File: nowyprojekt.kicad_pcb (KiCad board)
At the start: 4 copper layers, 75.6 x 70.8 mm, 46 parts, among them J1 Zasilanie, J2 01x03, J3 Conn_01x15_Pin, J4 Conn_01x15_Pin, Q1 BC856, Q2 BC856, Q3 BC856, Q4 BC856, U1 CA56-12SURKWA, U2 ATMEGA328P-AU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

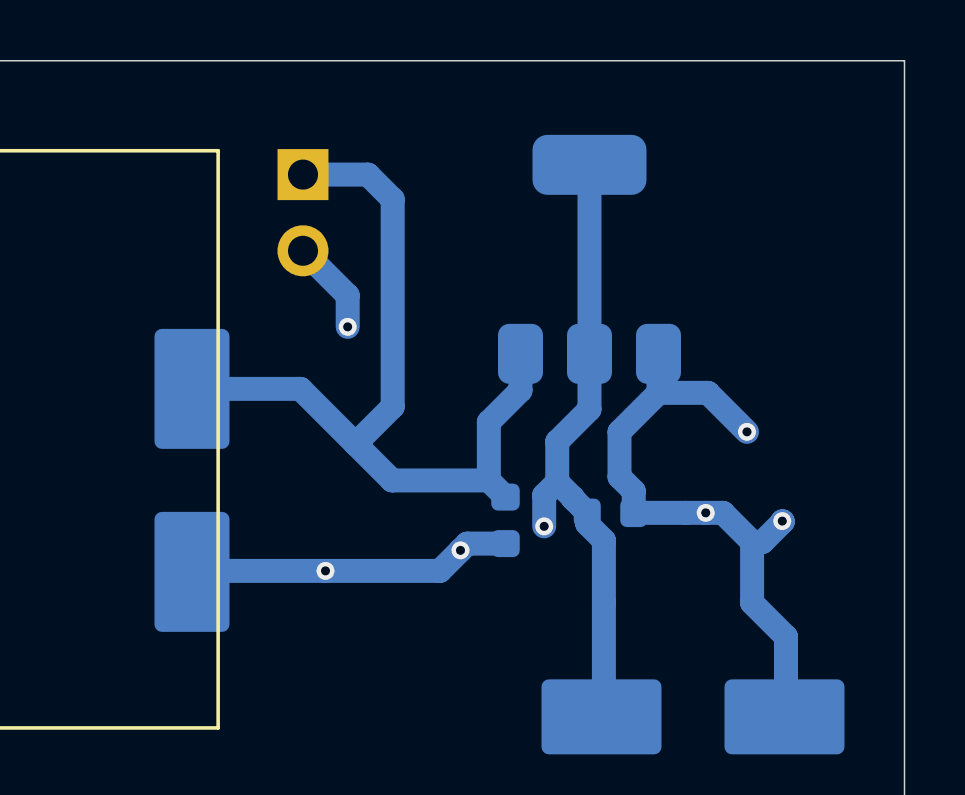
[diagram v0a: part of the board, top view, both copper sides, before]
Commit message: Inne rozwiazanie prowadzenia sciezek, z mysleniem zgodnym z 4 warstwami plytki... przelotki zasilania stabilizatora obok przelotek kondensatorow itd
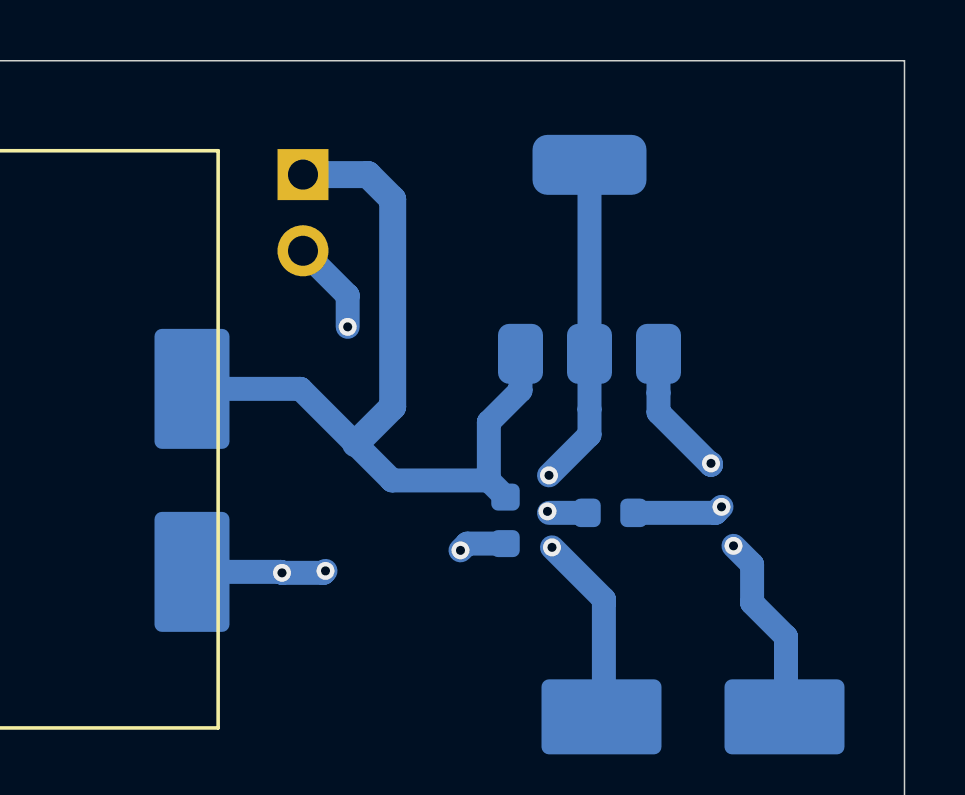
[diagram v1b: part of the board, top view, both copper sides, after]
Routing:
- net GND: track 82.9 -> 70.6 mm, vias 26 -> 27
- net +5V: track 66.7 -> 63.8 mm, vias 15 -> 17

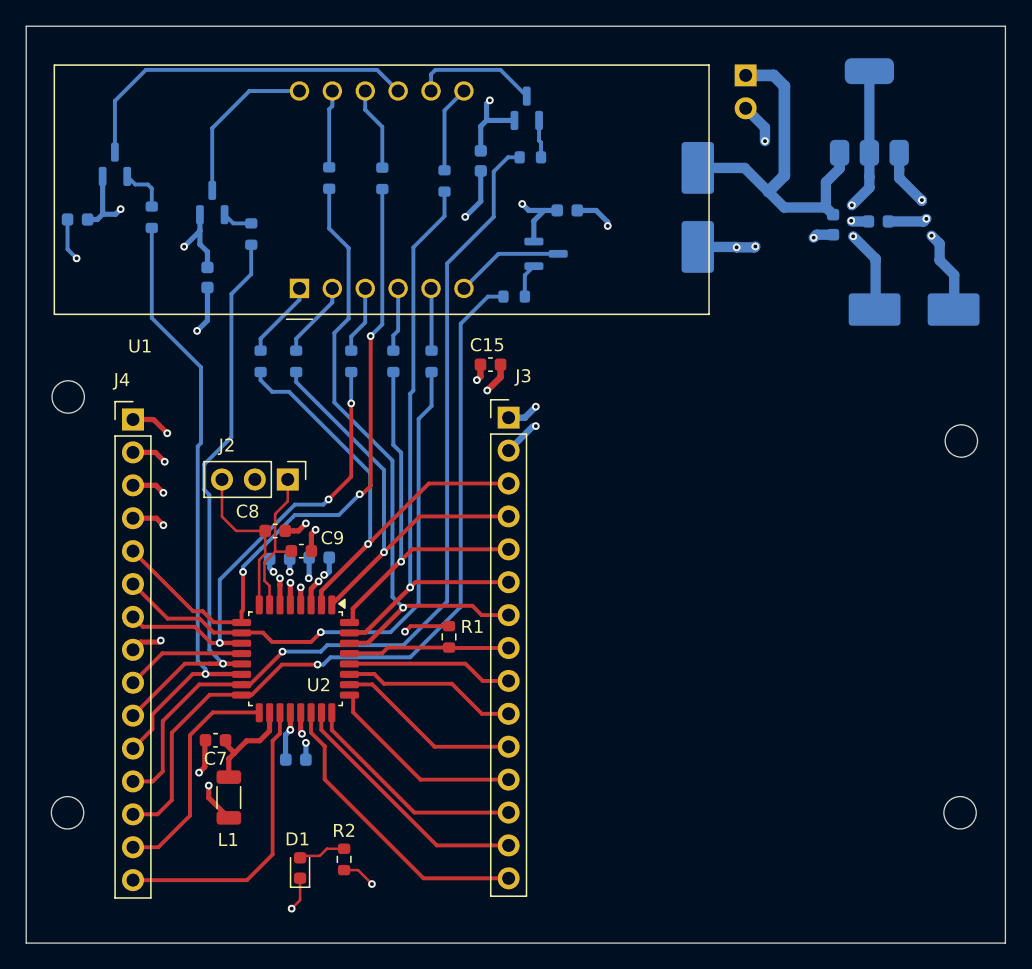
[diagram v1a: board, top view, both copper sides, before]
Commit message: 01.03.2026r zmiana prowadzenia sciezek - myslenie pod 4 warstwowe pcb
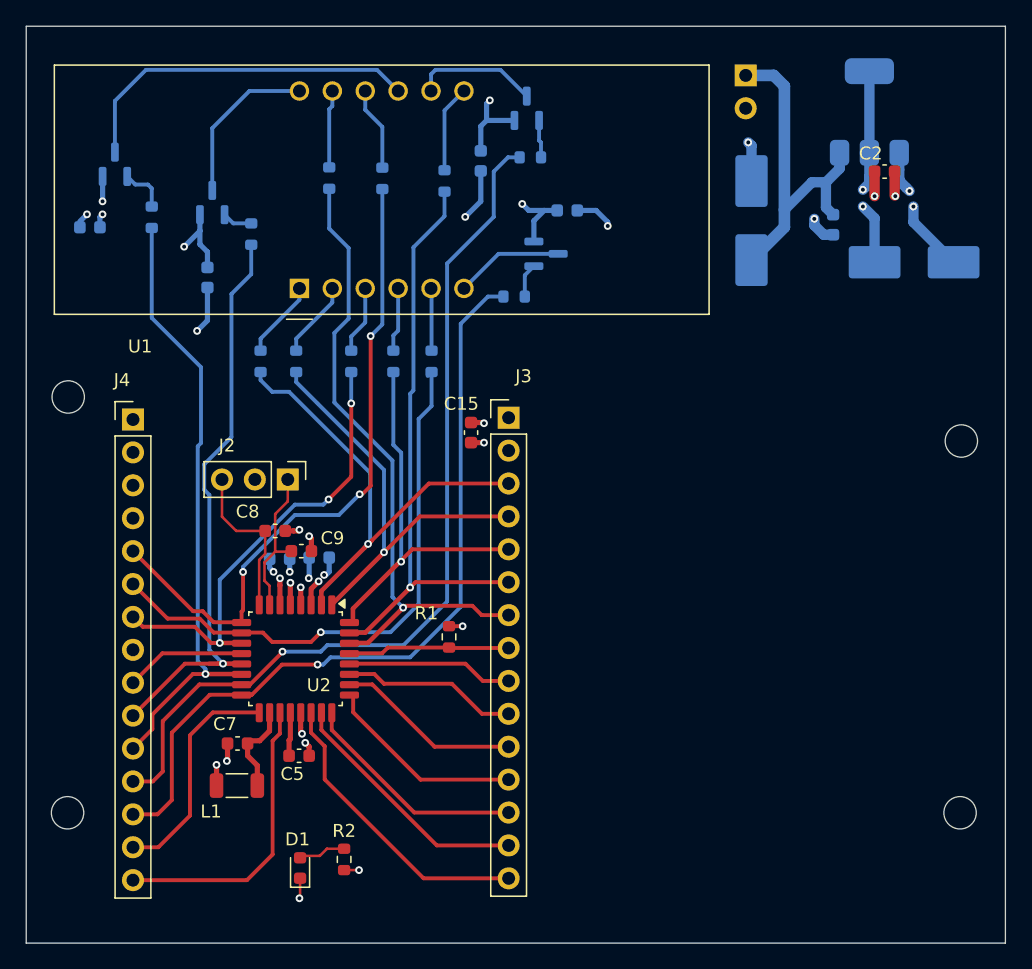
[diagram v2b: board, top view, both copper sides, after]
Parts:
- C2, C5: moved to F.Cu
- moved C15 5.46 mm to (191.2, 55.2), turned to -90 degrees
- moved C4 4.27 mm to (212.9, 38.9), turned to 90 degrees
- moved C2 3.88 mm to (223.2, 35.1)
- moved C3 3.65 mm to (225.4, 42.1)
- moved C7 1.72 mm to (173.2, 79.2)
- moved C11 1.12 mm to (161.8, 39.4)
- moved L1 1.11 mm to (173.2, 82.5), turned to 0 degrees
- moved C5 0.39 mm to (178.0, 80.2)
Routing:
- net GND: track 70.6 -> 43.5 mm, vias 27 -> 20
- net +5V: track 63.8 -> 48.1 mm, vias 17 -> 16
- net VIN: track 28.6 -> 27.3 mm
- net Net-(U2-AVCC): track 7.92 -> 7.06 mm
- net Net-(U2-AREF): track 3.93 -> 3.37 mm, vias 1 -> 0

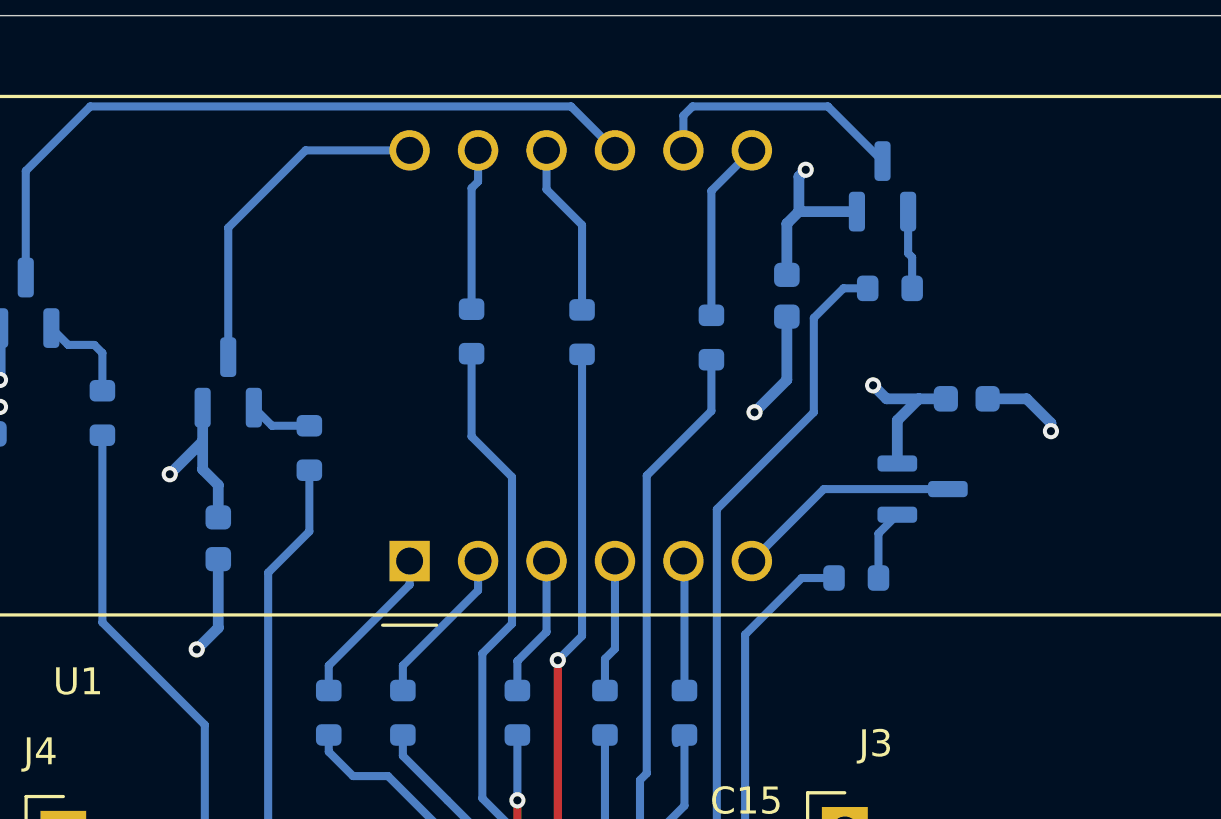
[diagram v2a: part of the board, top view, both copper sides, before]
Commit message: 01.03.2026r zmiana prowadzenia sciezek - myslenie pod 4 warstwowe pcb czesc 2 - zakonczenie
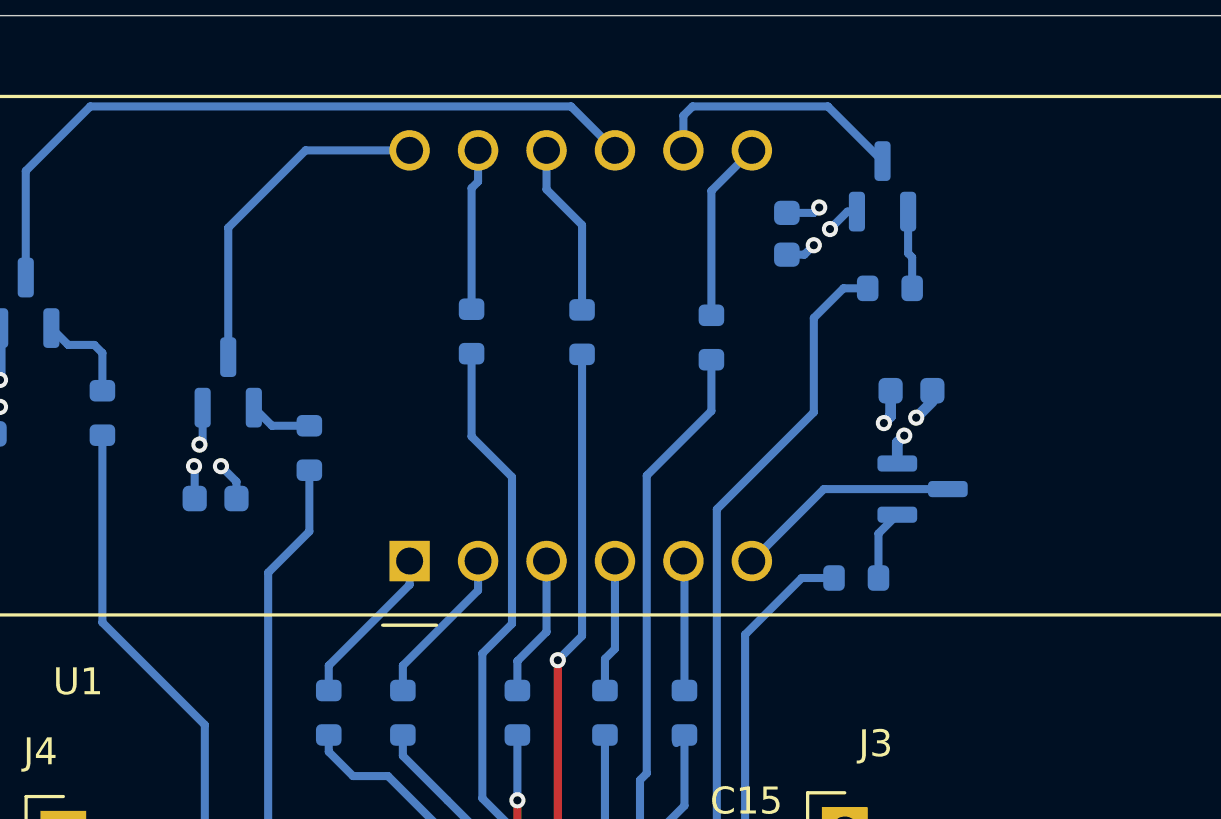
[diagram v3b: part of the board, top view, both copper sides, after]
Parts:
- moved C13 2.30 mm to (192.0, 32.0)
- moved C14 2.07 mm to (196.6, 37.8)
- moved C12 1.48 mm to (170.8, 41.8), turned to 0 degrees
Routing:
- net +5V: track 48.1 -> 37.7 mm, vias 16 -> 19
- net GND: track 43.5 -> 36.6 mm

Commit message: 06.03.2026 small update
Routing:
- net +5V: track 37.7 -> 38.5 mm
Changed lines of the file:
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@@
+	)
+	(segment
+		(start 194.15 54.1)
+		(end 194.9 54.1)
+		(width 0.2)
+		(layer "B.Cu")
+		(net 2)
 	)
 	(segment

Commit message: biggest update 06.03.2026r
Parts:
- moved C1 1.97 mm to (220.0, 37.4)
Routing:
- net VIN: track 27.3 -> 26.5 mm
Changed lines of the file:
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@@
 	(footprint "Capacitor_SMD:C_0603_1608Metric"
 		(layer "B.Cu")
-		(at 219.2 39.2 -90)
+		(at 220 37.4 -90)
 		(descr "Capacitor SMD 0603 (1608 Metric), square (rectangular) end terminal, IPC-7351 nominal, (Body size source: IPC-SM-782 page 76, https://www.pcb-3d.com/wordpress/wp-content/uploads/ipc-sm-782a_amendment_1_and_2.pdf), generated with kicad-footprint-generator")
 		(tags "capacitor")
 		(property "Reference" "C1"
-			(at 2.3 0.45 0)
+			(at 2.2 0 0)
 			(layer "B.SilkS")
 			(effects
@@
 	)
 	(segment
-		(start 218.645 35.925)
-		(end 218.645 37.87)
+		(start 219.7 34.87)
+		(end 219.7 35.7)
 		(width 0.8)
 		(layer "B.Cu")
@@
 	)
 	(segment
+		(start 220 36)
+		(end 220 36.625)
+		(width 0.8)
+		(layer "B.Cu")
+		(net 1)
+	)
+	(segment
 		(start 212.45 27.675)
 		(end 214.615 27.675)
@@
 	)
 	(segment
+		(start 219.7 35.7)
+		(end 220 36)
+		(width 0.8)
+		(layer "B.Cu")
+		(net 1)
+	)
+	(segment
 		(start 218.645 35.925)
 		(end 217.565 35.925)
-		(width 0.8)
-		(layer "B.Cu")
-		(net 1)
-	)
-	(segment
-		(start 218.645 37.87)
-		(end 219.2 38.425)
 		(width 0.8)
 		(layer "B.Cu")
@@
 	)
 	(via
-		(at 217.75 38.75)
-		(size 0.6)
-		(drill 0.3)
-		(layers "F.Cu" "B.Cu")
-		(net 3)
-	)
-	(via
 		(at 225.1 36.6)
 		(size 0.6)
@@
 	(via
 		(at 193 32.4)
+		(size 0.6)
+		(drill 0.3)
+		(layers "F.Cu" "B.Cu")
+		(net 3)
+	)
+	(via
+		(at 218.4 37.6)
 		(size 0.6)
 		(drill 0.3)
@@
 	)
 	(segment
-		(start 217.75 39.25)
-		(end 217.75 38.75)
+		(start 220 38.175)
+		(end 219.175 38.175)
+		(width 0.8)
+		(layer "B.Cu")
+		(net 3)
+	)
+	(segment
+		(start 218.975 38.175)
+		(end 218.4 37.6)
+		(width 0.8)
+		(layer "B.Cu")
+		(net 3)
+	)
+	(segment
+		(start 219.175 38.175)
+		(end 218.975 38.175)
 		(width 0.8)
 		(layer "B.Cu")
@@
 	)
 	(segment
-		(start 218.475 39.975)
-		(end 217.75 39.25)
-		(width 0.8)
-		(layer "B.Cu")
-		(net 3)
-	)
-	(segment
 		(start 228.5 42.1)
 		(end 225.4 39)
@@
 		(layer "B.Cu")
 		(net 3)
-	)
-	(segment
-		(start 219.2 39.975)
-		(end 218.475 39.975)
-		(width 0.8)
-		(layer "B.Cu")
-		(net 3)

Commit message: 07.03.2026r update LISTA BOM itd
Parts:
- R2: value 680 -> 680R
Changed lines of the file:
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@@
 			(plot_on_all_layers_selection 0x00000000_00000000_00000000_00000000)
 			(disableapertmacros no)
-			(usegerberextensions no)
+			(usegerberextensions yes)
 			(usegerberattributes yes)
 			(usegerberadvancedattributes yes)
@@
 			(drillshape 0)
 			(scaleselection 1)
-			(outputdirectory "C:/Users/Filip Gamer/Documents/projektkicad/nowyprojekt")
+			(outputdirectory "C:/Users/Filip Gamer/Documents/projektkicad/nowyprojekt/gerbery_produkcja")
 		)
 	)
@@
 			)
 		)
-		(property "Value" "680"
+		(property "Value" "680R"
 			(at 2.4 -0.95 0)
 			(layer "F.Fab")
